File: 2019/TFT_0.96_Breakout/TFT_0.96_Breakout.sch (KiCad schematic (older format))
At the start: 4 parts

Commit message: Add tft-shield project
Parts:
- J?: symbol Connector:Conn_01x11_Female -> TFT_0.96_Breakout-rescue:Conn_01x11_Female-Connector
- Q?: symbol Transistor_BJT:PN2222A -> TFT_0.96_Breakout-rescue:PN2222A-Transistor_BJT
- U?: symbol Reference_Voltage:ISL21070CIH325Z-TK -> TFT_0.96_Breakout-rescue:ISL21070CIH325Z-TK-Reference_Voltage
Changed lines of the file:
@@
-EESchema Schematic File Version 5
+EESchema Schematic File Version 4
 LIBS:TFT_0.96_Breakout-cache
 EELAYER 29 0
@@
 CS
 $Comp
-L Connector:Conn_01x11_Female J?
+L TFT_0.96_Breakout-rescue:Conn_01x11_Female-Connector J?
 U 1 1 5CCE5396
 P 6875 3600
@@
 $EndComp
 $Comp
-L Transistor_BJT:PN2222A Q?
+L TFT_0.96_Breakout-rescue:PN2222A-Transistor_BJT Q?
 U 1 1 5CCE6CED
 P 7025 5375
@@
 $EndComp
 $Comp
-L Reference_Voltage:ISL21070CIH325Z-TK U?
+L TFT_0.96_Breakout-rescue:ISL21070CIH325Z-TK-Reference_Voltage U?
 U 1 1 5CCE9112
 P 5475 5600

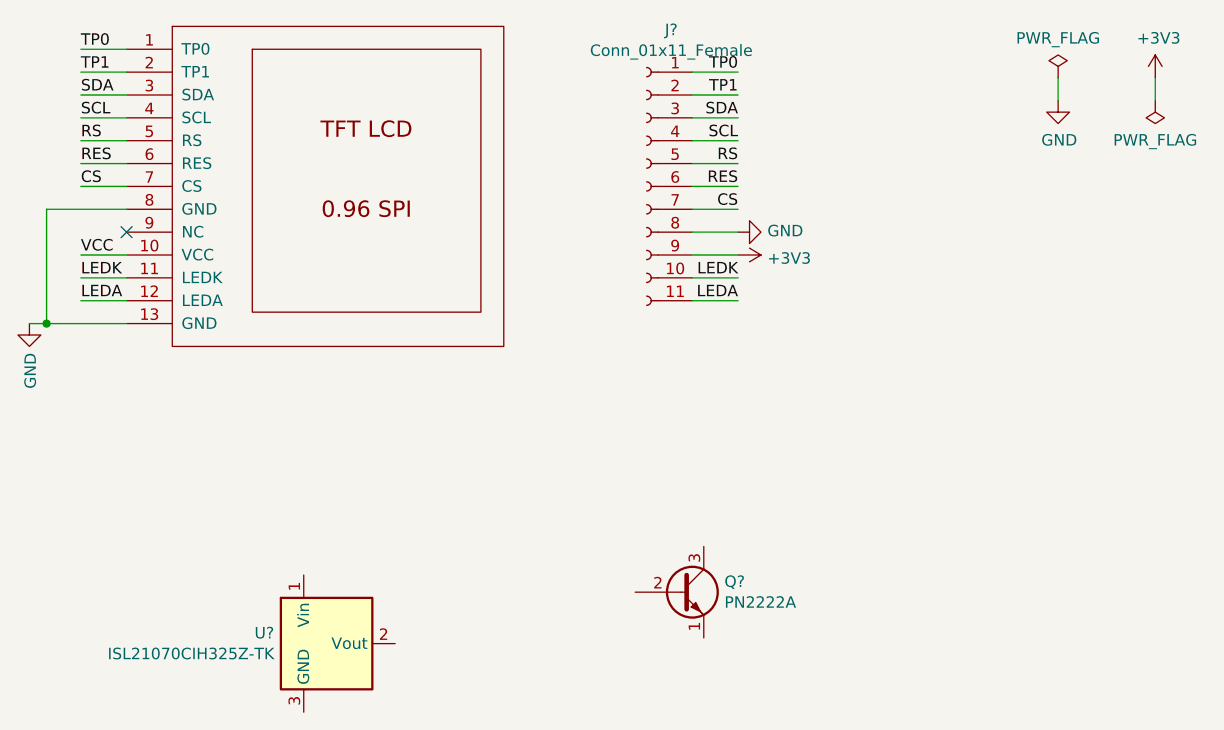
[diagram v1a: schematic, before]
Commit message: Add Draw settings in Docs TFT
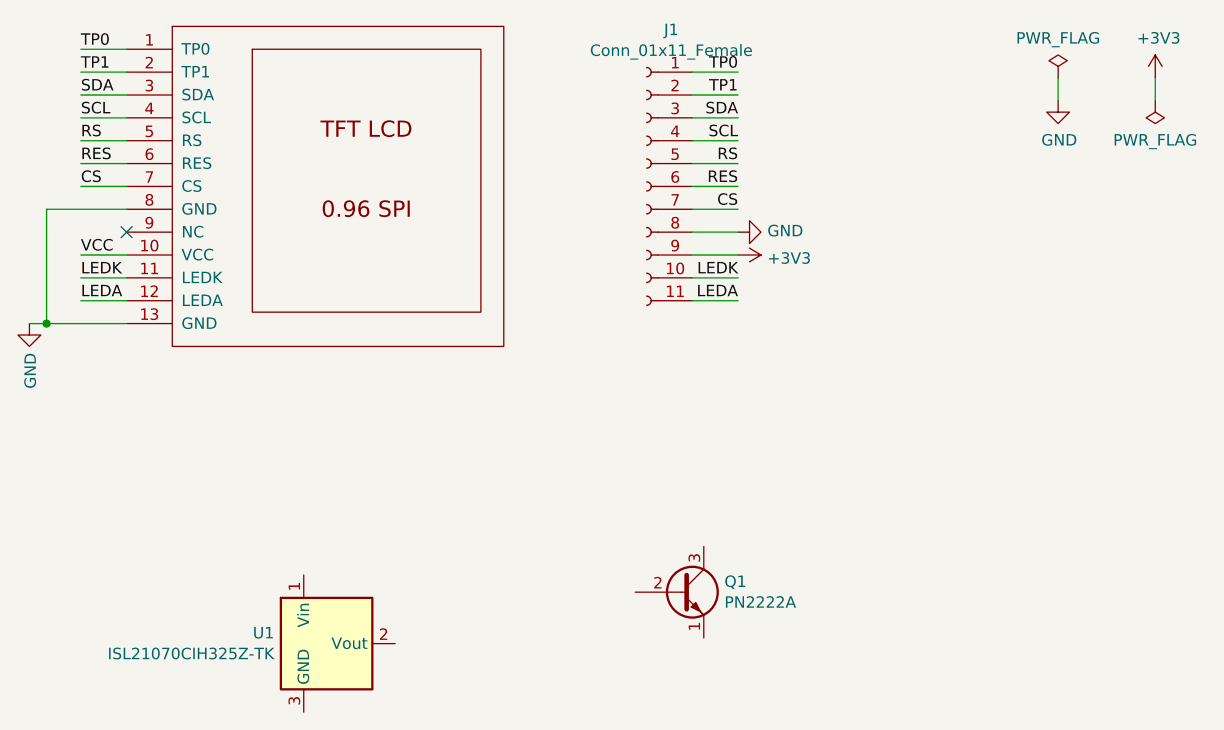
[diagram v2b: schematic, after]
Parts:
- U2: renamed from U?; footprint (none) -> TFT_0.96_Breakout:TFT_0.96_SPI
- gave numbers to parts that had none: 3
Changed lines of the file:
@@
 	4175 4200 4250 4200
 $Comp
-L TFT_0.96_Breakout:LCD_0.96_SPI U?
+L TFT_0.96_Breakout:LCD_0.96_SPI U2
 U 1 1 5CCE97B7
 P 5500 3500
-F 0 "U?" H 5550 4350 50  0001 C CNN
+F 0 "U2" H 5550 4350 50  0001 C CNN
 F 1 "LCD_0.96_SPI" H 5500 2550 50  0001 C CNN
-F 2 "" H 5500 2550 50  0001 C CNN
+F 2 "TFT_0.96_Breakout:TFT_0.96_SPI" H 5500 2550 50  0001 C CNN
 F 3 "" H 5500 2550 50  0001 C CNN
 	1    5500 3500
@@
 CS
 $Comp
-L TFT_0.96_Breakout-rescue:Conn_01x11_Female-Connector J?
+L TFT_0.96_Breakout-rescue:Conn_01x11_Female-Connector J1
 U 1 1 5CCE5396
 P 6875 3600
-F 0 "J?" H 6767 4285 50  0000 C CNN
+F 0 "J1" H 6767 4285 50  0000 C CNN
 F 1 "Conn_01x11_Female" H 6767 4194 50  0000 C CNN
 F 2 "" H 6875 3600 50  0001 C CNN
@@
 LEDA
 $Comp
-L power:PWR_FLAG #FLG?
+L power:PWR_FLAG #FLG0101
 U 1 1 5CCEB908
 P 8675 3125
-F 0 "#FLG?" H 8675 3200 50  0001 C CNN
+F 0 "#FLG0101" H 8675 3200 50  0001 C CNN
 F 1 "PWR_FLAG" H 8675 3298 50  0000 C CNN
 F 2 "" H 8675 3125 50  0001 C CNN
@@
 $EndComp
 $Comp
-L power:PWR_FLAG #FLG?
+L power:PWR_FLAG #FLG0102
 U 1 1 5CCEC08C
 P 9100 3225
-F 0 "#FLG?" H 9100 3300 50  0001 C CNN
+F 0 "#FLG0102" H 9100 3300 50  0001 C CNN
 F 1 "PWR_FLAG" H 9100 3398 50  0000 C CNN
 F 2 "" H 9100 3225 50  0001 C CNN
@@
 $EndComp
 $Comp
-L power:+3V3 #PWR?
+L power:+3V3 #PWR0101
 U 1 1 5CCE56EB
 P 9100 3125
-F 0 "#PWR?" H 9100 2975 50  0001 C CNN
+F 0 "#PWR0101" H 9100 2975 50  0001 C CNN
 F 1 "+3V3" H 9115 3298 50  0000 C CNN
 F 2 "" H 9100 3125 50  0001 C CNN
@@
 	9100 3225 9100 3125
 $Comp
-L power:+3V3 #PWR?
+L power:+3V3 #PWR0102
 U 1 1 5CCE7047
 P 7275 3900
-F 0 "#PWR?" H 7275 3750 50  0001 C CNN
+F 0 "#PWR0102" H 7275 3750 50  0001 C CNN
 F 1 "+3V3" V 7290 4028 50  0000 L CNN
 F 2 "" H 7275 3900 50  0001 C CNN
@@
 $EndComp
 $Comp
-L power:GND #PWR?
+L power:GND #PWR0103
 U 1 1 5CCE93D2
 P 8675 3225
-F 0 "#PWR?" H 8675 2975 50  0001 C CNN
+F 0 "#PWR0103" H 8675 2975 50  0001 C CNN
 F 1 "GND" H 8680 3052 50  0000 C CNN
 F 2 "" H 8675 3225 50  0001 C CNN
@@
 $EndComp
 $Comp
-L power:GND #PWR?
+L power:GND #PWR0104
 U 1 1 5CCE9A39
 P 7275 3800
-F 0 "#PWR?" H 7275 3550 50  0001 C CNN
+F 0 "#PWR0104" H 7275 3550 50  0001 C CNN
 F 1 "GND" V 7280 3672 50  0000 R CNN
 F 2 "" H 7275 3800 50  0001 C CNN
@@
 	4250 4200 4600 4200
 $Comp
-L power:GND #PWR?
+L power:GND #PWR0105
 U 1 1 5CCE59DE
 P 4175 4200
-F 0 "#PWR?" H 4175 3950 50  0001 C CNN
+F 0 "#PWR0105" H 4175 3950 50  0001 C CNN
 F 1 "GND" V 4180 4072 50  0000 R CNN
 F 2 "" H 4175 4200 50  0001 C CNN
@@
 $EndComp
 $Comp
-L TFT_0.96_Breakout-rescue:PN2222A-Transistor_BJT Q?
+L TFT_0.96_Breakout-rescue:PN2222A-Transistor_BJT Q1
 U 1 1 5CCE6CED
 P 7025 5375
-F 0 "Q?" H 7215 5421 50  0000 L CNN
+F 0 "Q1" H 7215 5421 50  0000 L CNN
 F 1 "PN2222A" H 7215 5330 50  0000 L CNN
 F 2 "Package_TO_SOT_THT:TO-92_Inline" H 7225 5300 50  0001 L CIN
@@
 $EndComp
 $Comp
-L TFT_0.96_Breakout-rescue:ISL21070CIH325Z-TK-Reference_Voltage U?
+L TFT_0.96_Breakout-rescue:ISL21070CIH325Z-TK-Reference_Voltage U1
 U 1 1 5CCE9112
 P 5475 5600
-F 0 "U?" H 5246 5646 50  0000 R CNN
+F 0 "U1" H 5246 5646 50  0000 R CNN
 F 1 "ISL21070CIH325Z-TK" H 5246 5555 50  0000 R CNN
 F 2 "Package_TO_SOT_SMD:SOT-23" H 5975 5350 50  0001 C CIN
